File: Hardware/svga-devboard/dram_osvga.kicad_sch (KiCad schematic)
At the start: 2 parts

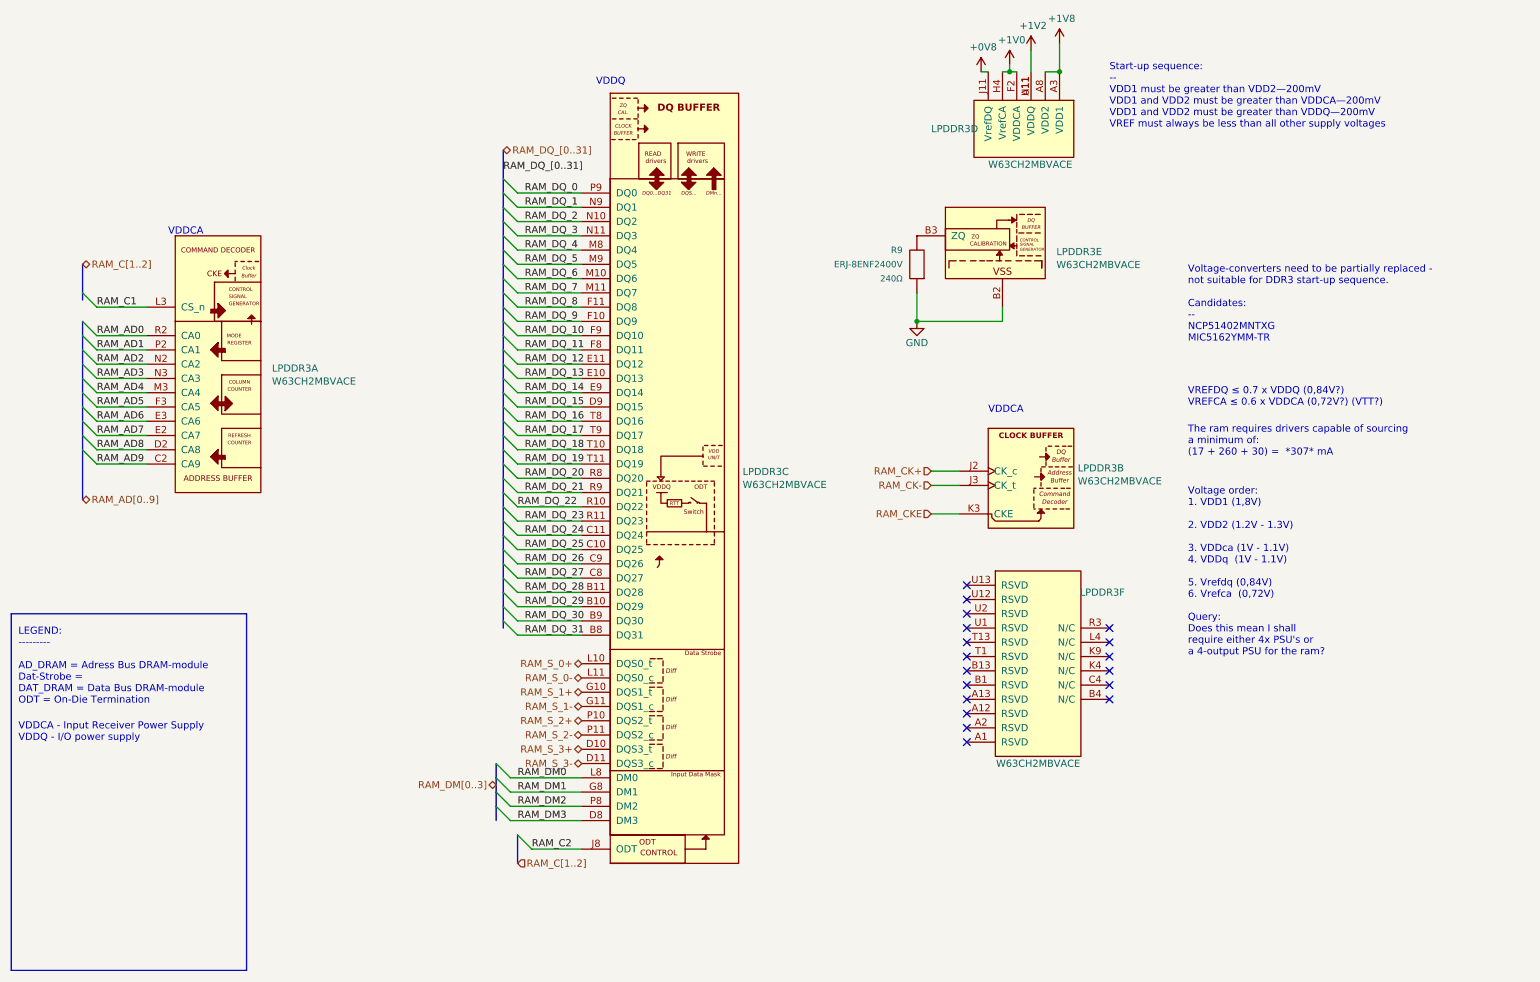
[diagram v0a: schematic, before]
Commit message: Disconnected the DVI-connectors from each other, so that they do go over the intended flat-cable to the daughter-board instead.
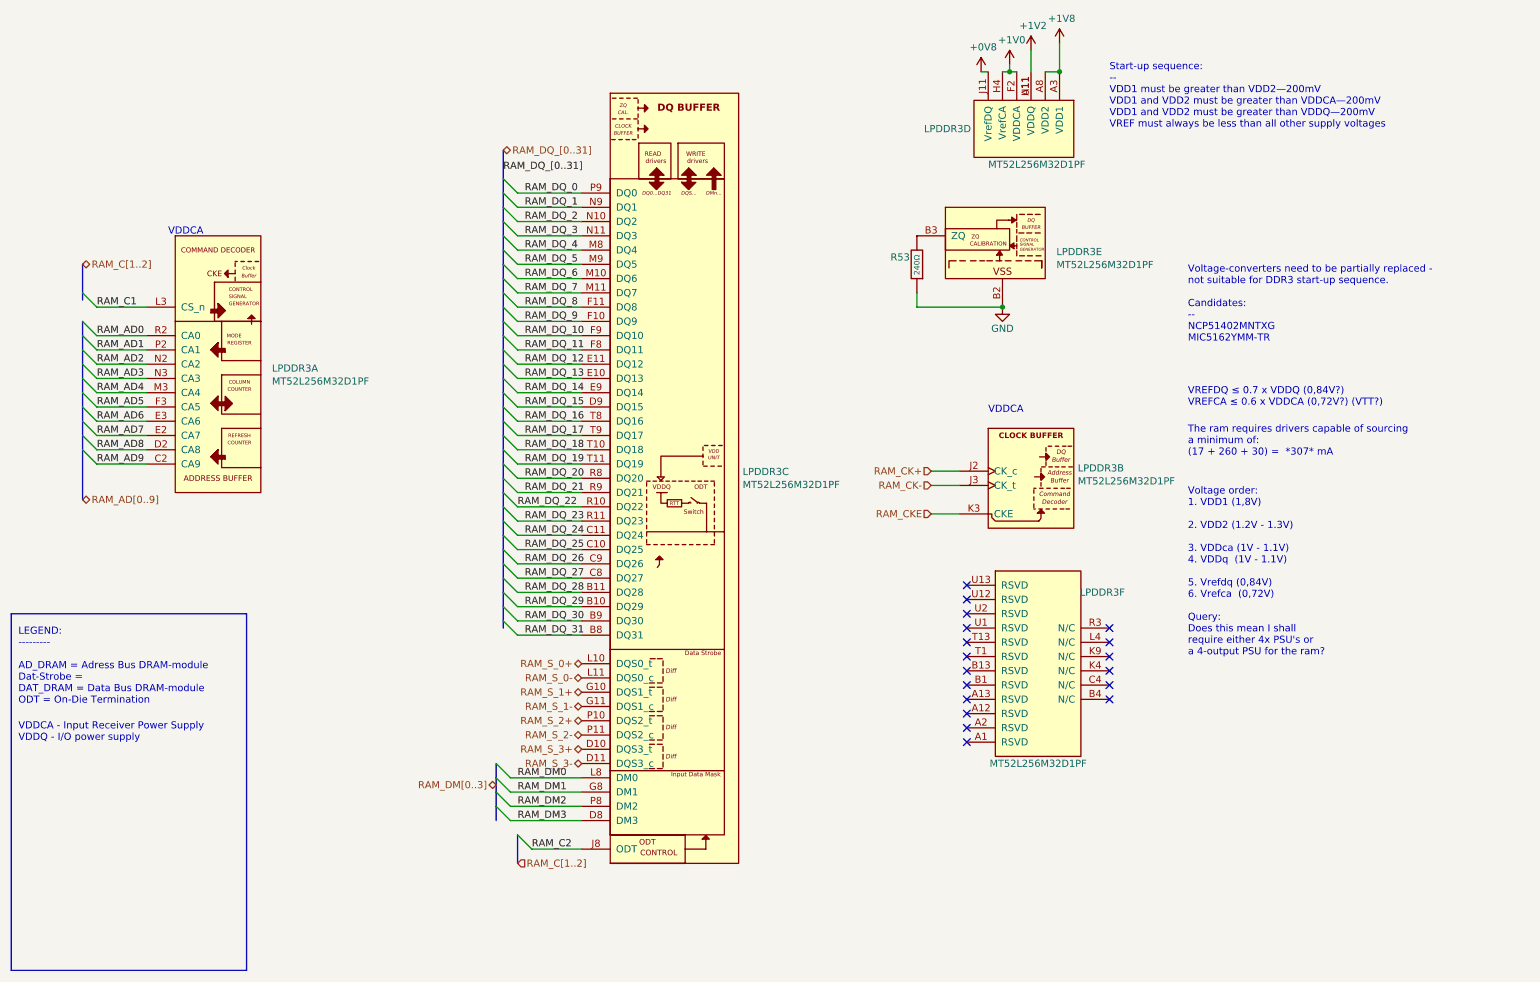
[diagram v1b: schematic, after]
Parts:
- removed R9: ERJ-8ENF2400V, Resistor_SMD:R_1206_3216Metric, symbol LRJ-parts:R_ERJ-8ENF2400V
- added R53: R_RT0603FRE07240RL, LRJ:R_0603_1608Metric_roundcourt, symbol LRJ-parts:R_RT0603FRE07240RL
- LPDDR3: value W63CH2MBVACE -> MT52L256M32D1PF; footprint Footprints:Winbond_VFBGA-178_W63CH2MBVACE -> LRJ:Micron_VFBGA-178_11x11.5mm_Layout11.5x11.7_P0.65mm; symbol LRJ-parts:W63CH2MBVACE -> LRJ-parts:Micron_MT52L256M32D1PF; MPN (none) -> MT52L256M32D1PF-107 WT:B; Manufacturer Winbond Electronics Corporation -> Micron Technology Inc.; Operating temperature (none) -> -30°C ~ 85°C; Status (none) -> Active; Voltage rating (none) -> 1.3V
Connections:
- net GND: now also R53.2
- net at LPDDR3.B3 (ZQ): now also R53.1
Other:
- note removed: "VDDQ"
